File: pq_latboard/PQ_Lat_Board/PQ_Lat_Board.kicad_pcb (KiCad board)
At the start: 6 copper layers, 48 x 48 mm, 19 parts, among them IC1 TCN75AVOA713, J1 Conn_01x11_MountingPin, J2 connector-coax

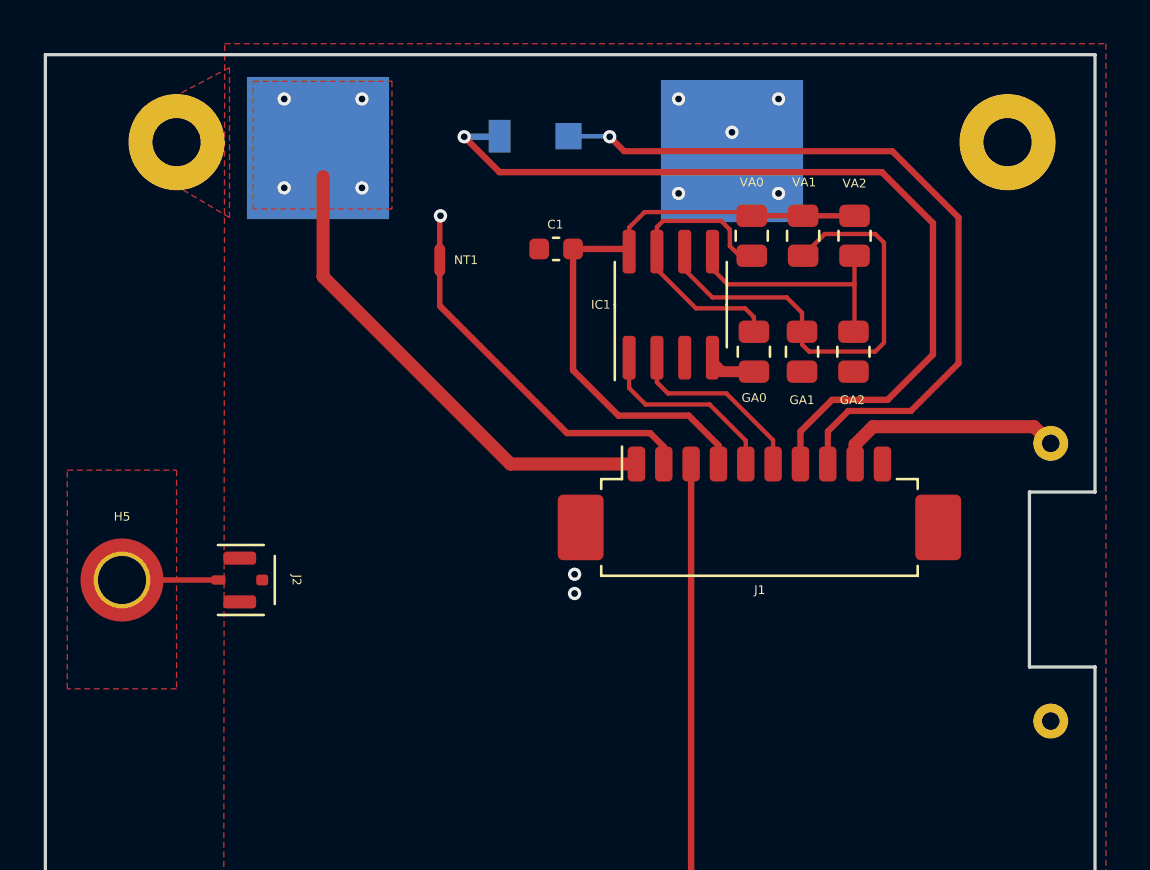
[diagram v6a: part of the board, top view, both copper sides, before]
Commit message: Full Kicad7 transition, library improvement and adaptation, correct footprints and 3D models added
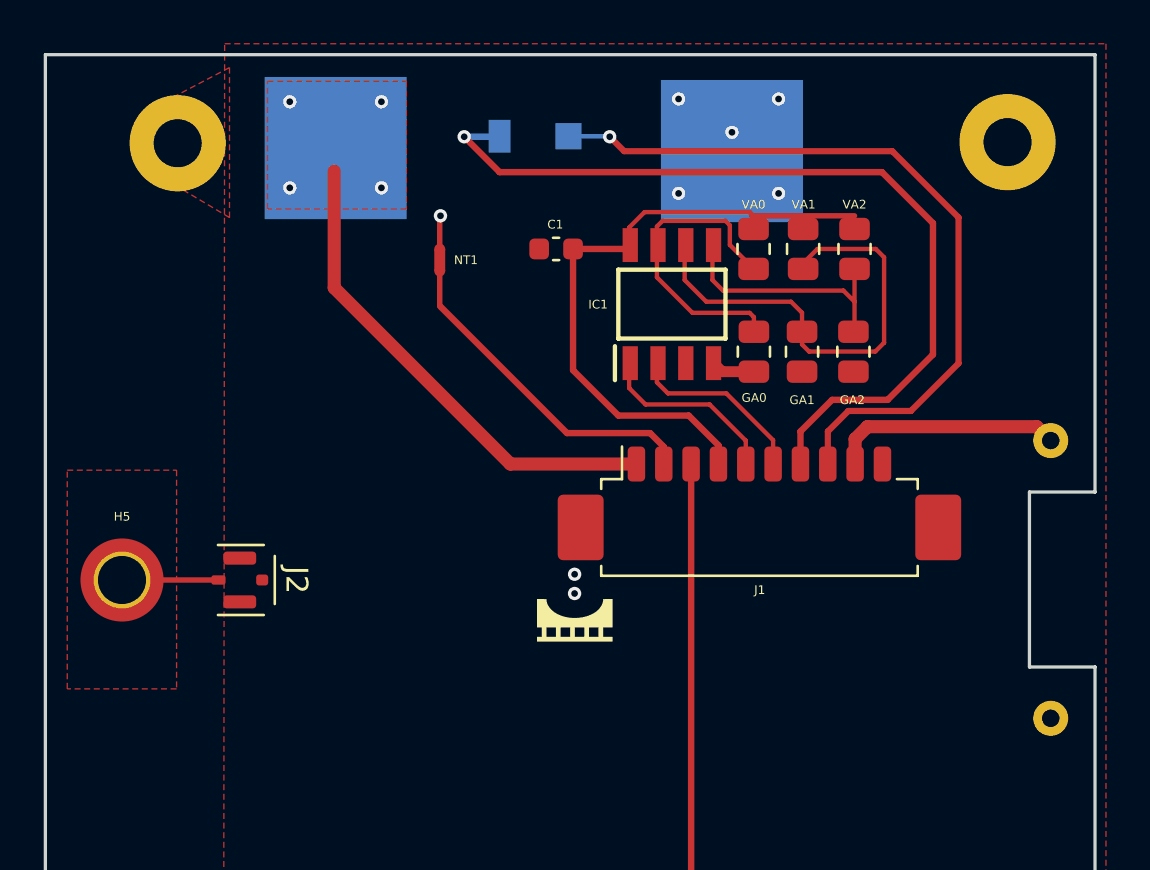
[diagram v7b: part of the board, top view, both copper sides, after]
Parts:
- added Annotation1: Silkscreen_Annotation, -nsl_symbols:Bridgemaker, F.Cu at (99.3, 67.8)
- D1: footprint passive-nsl:SLCD-61N8 -> -nsl_passive:SLCD-61N8
- IC1: footprint Package_SO:SOP-8_3.9x4.9mm_P1.27mm -> -nsl_sensor:TCN75AVOA
- J2: footprint connector-nsl:C.FL-R-SMT-1(90) -> -nsl_connector:C.FL-R-SMT-1(90)
- SC1: footprint power-nsl:Azur-Space-PQ-cut-SC -> -nsl_power:Azur-Space-PQ-cut-SC
- moved VA0 0.61 mm to (107.4, 50.9)
- moved VA1 0.60 mm to (109.7, 50.9)
- moved VA2 0.60 mm to (112.0, 50.9)
- moved THT1 0.13 mm to (121.0, 59.6)
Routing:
- net Net-(IC1-A0): track 12.9 -> 14.2 mm

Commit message: fabrication
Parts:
- moved SC1 0.59 mm to (100.5, 68.7)
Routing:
- net GND: vias 5 -> 4
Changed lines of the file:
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@@
   )
   (footprint "-nsl_power:Azur-Space-PQ-cut-SC" (layer "B.Cu")
-    (at 100.4676 69.26975 180)
+    (at 100.4676 68.675 180)
     (property "Sheetfile" "PQ_Lat_Board.kicad_sch")
     (property "Sheetname" "")
@@
     (fp_line (start -17.78 19.68) (end -17.78 -20.32)
       (stroke (width 0.293) (type solid)) (layer "B.SilkS"))
-    (fp_line (start -17.78 19.68) (end -10.16 19.685)
+    (fp_line (start -17.78 19.68) (end -11 19.685)
       (stroke (width 0.3) (type solid)) (layer "B.SilkS"))
-    (fp_line (start -1.27 19.685) (end 7.366 19.685)
+    (fp_line (start -1.1 19.685) (end 7.1 19.685)
       (stroke (width 0.3) (type solid)) (layer "B.SilkS"))
     (fp_line (start 17.145 19.68) (end 18.22 19.68)
@@
     (fp_line (start 18.22 19.68) (end 18.22 -20.32)
       (stroke (width 0.293) (type solid)) (layer "B.SilkS"))
-    (pad "1" smd rect (at -5.93 22.86 180) (size 6.5 6.5) (layers "B.Cu" "B.Paste" "B.Mask")
+    (pad "1" smd rect (at -5.9 21.8 180) (size 8.4 4.4) (layers "B.Cu" "B.Paste" "B.Mask")
       (net 9 "GND") (pinfunction "-") (pintype "passive"))
-    (pad "2" smd rect (at 12.192 23 180) (size 6.5 6.5) (layers "B.Cu" "B.Paste" "B.Mask")
+    (pad "2" smd rect (at 12.2 21.875 180) (size 8.4 4.25) (layers "B.Cu" "B.Paste" "B.Mask")
       (net 10 "/SOLAR") (pintype "passive"))
     (model "${KICAD_NSL_DIR}/power-nsl/StepFiles/TJ_Solar_Cell_Assembly_3G30A_PQcut_coloured.step"
@@
   (segment (start 105.9435 56.4955) (end 105.505 56.057) (width 0.5) (layer "F.Cu") (net 9))
   (segment (start 107.201 56.4955) (end 105.9435 56.4955) (width 0.5) (layer "F.Cu") (net 9))
-  (via (at 106.3976 45.55) (size 0.61) (drill 0.305) (layers "F.Cu" "B.Cu") (net 9))
   (via (at 108.528 48.344) (size 0.61) (drill 0.305) (layers "F.Cu" "B.Cu") (net 9))
-  (via (at 108.528 44.026) (size 0.61) (drill 0.305) (layers "F.Cu" "B.Cu") (net 9))
+  (via (at 108.528 45.2) (size 0.61) (drill 0.305) (layers "F.Cu" "B.Cu") (net 9))
   (via (at 103.956 48.344) (size 0.61) (drill 0.305) (layers "F.Cu" "B.Cu") (net 9))
-  (via (at 103.956 44.026) (size 0.61) (drill 0.305) (layers "F.Cu" "B.Cu") (net 9))
+  (via (at 103.956 45.2) (size 0.61) (drill 0.305) (layers "F.Cu" "B.Cu") (net 9))
   (segment (start 102.028617 60.718784) (end 96.264784 60.718784) (width 0.6) (layer "F.Cu") (net 10))
   (segment (start 96.264784 60.718784) (end 88.208 52.662) (width 0.6) (layer "F.Cu") (net 10))
   (segment (start 88.208 52.662) (end 88.208 47.328) (width 0.6) (layer "F.Cu") (net 10))
-  (via (at 86.176 48.09) (size 0.61) (drill 0.305) (layers "F.Cu" "B.Cu") (net 10))
+  (via (at 88.2676 46.8) (size 0.61) (drill 0.305) (layers "F.Cu" "B.Cu") (net 10))
   (via (at 90.367 48.09) (size 0.61) (drill 0.305) (layers "F.Cu" "B.Cu") (net 10))
-  (via (at 90.367 44.153) (size 0.61) (drill 0.305) (layers "F.Cu" "B.Cu") (net 10))
-  (via (at 86.176 44.153) (size 0.61) (drill 0.305) (layers "F.Cu" "B.Cu") (net 10))
+  (via (at 90.367 45.2) (size 0.61) (drill 0.305) (layers "F.Cu" "B.Cu") (net 10))
+  (via (at 86.176 45.247) (size 0.61) (drill 0.305) (layers "F.Cu" "B.Cu") (net 10))
   (segment (start 93.034 49.402) (end 93.068 49.368) (width 0.25) (layer "F.Cu") (net 11))
   (segment (start 93.034 50.892) (end 93.034 49.402) (width 0.25) (layer "F.Cu") (net 11))
@@
     (polygon
       (pts
-        (xy 91.51 49.0552)
-        (xy 85.16 49.0552)
-        (xy 85.16 43.2132)
-        (xy 91.51 43.2132)
+        (xy 92.41 48.9552)
+        (xy 84.06 48.9552)
+        (xy 84.06 44.7132)
+        (xy 92.41 44.7132)
       )
     )
@@
     (connect_pads (clearance 0.4))
     (min_thickness 0.254) (filled_areas_thickness no)
-    (fill yes (thermal_gap 0.508) (thermal_bridge_width 2))
+    (fill yes (thermal_gap 0.5) (thermal_bridge_width 1))
     (polygon
       (pts
